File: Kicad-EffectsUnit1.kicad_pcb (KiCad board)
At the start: 2 copper layers, 100 x 100 mm, 175 parts, among them J101 In7, J102 Doepfer connector, J104 In6, J105 In3, J106 Out10, J107 Out11, J108 Out9, J109 Out6, J201 In, J202 Out, J203 Conn_01x02_Male, P201 HEADER_2x5_Doepfer, P301 HEADER_2x5_Doepfer, Q201 BC337, Q202 PZT2222A, Q203 PZT2222A, Q301 BC337, SW101 Dist 6, SW102 Crush A6, SW104 Rotary_Encoder_Switch, SW105 Dist 10, U101 TL072, U102 TL072, U201 L7805, U202 PT2399

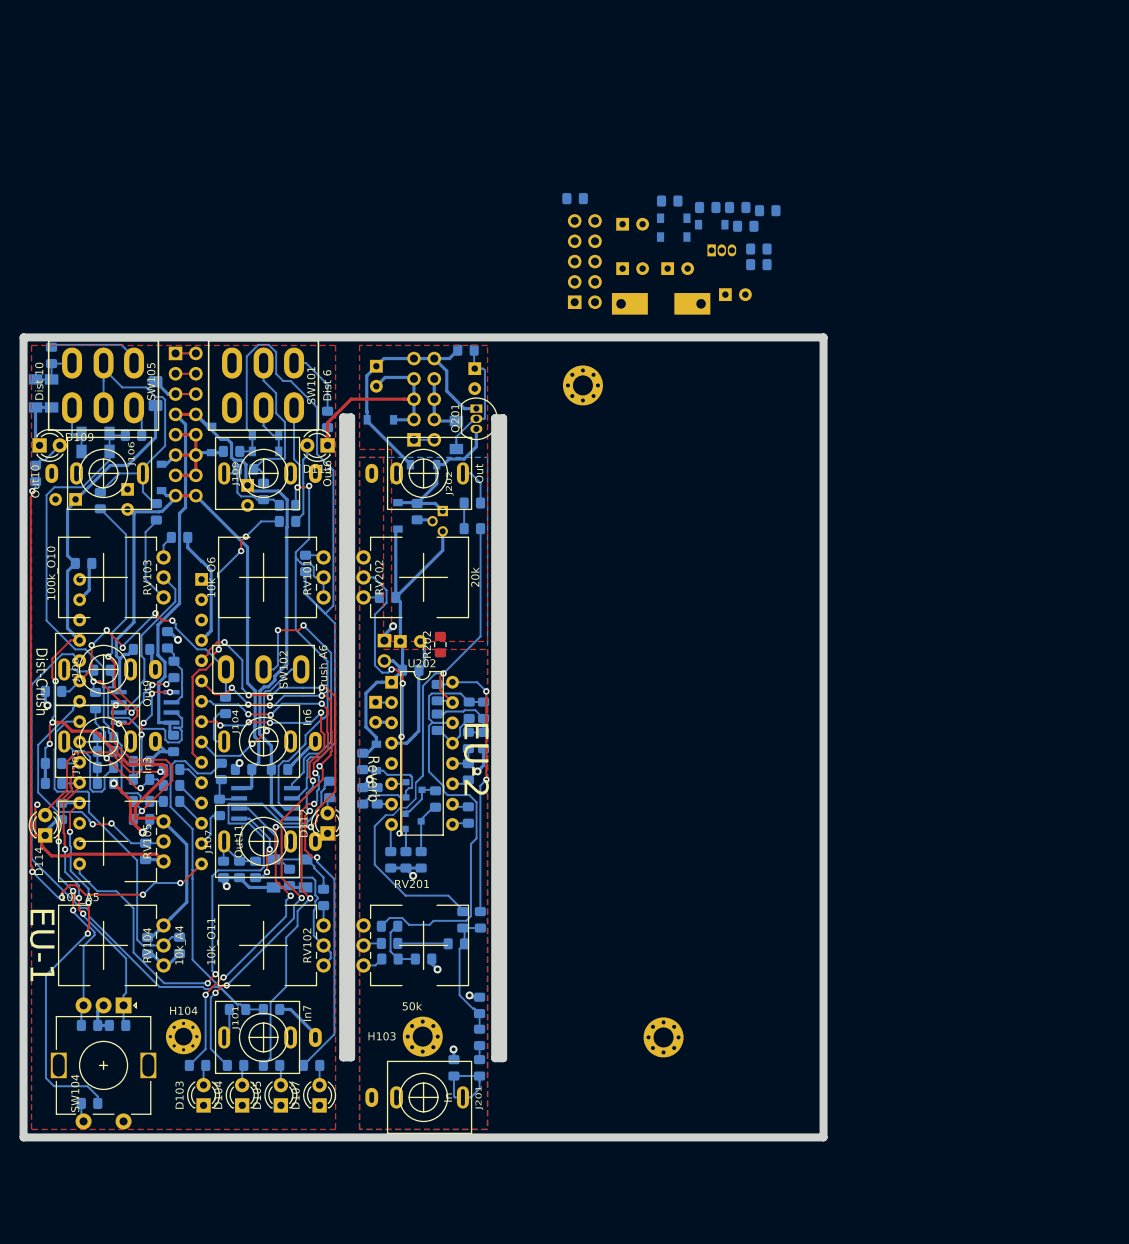
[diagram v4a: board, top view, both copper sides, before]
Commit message: Large components placed EU3
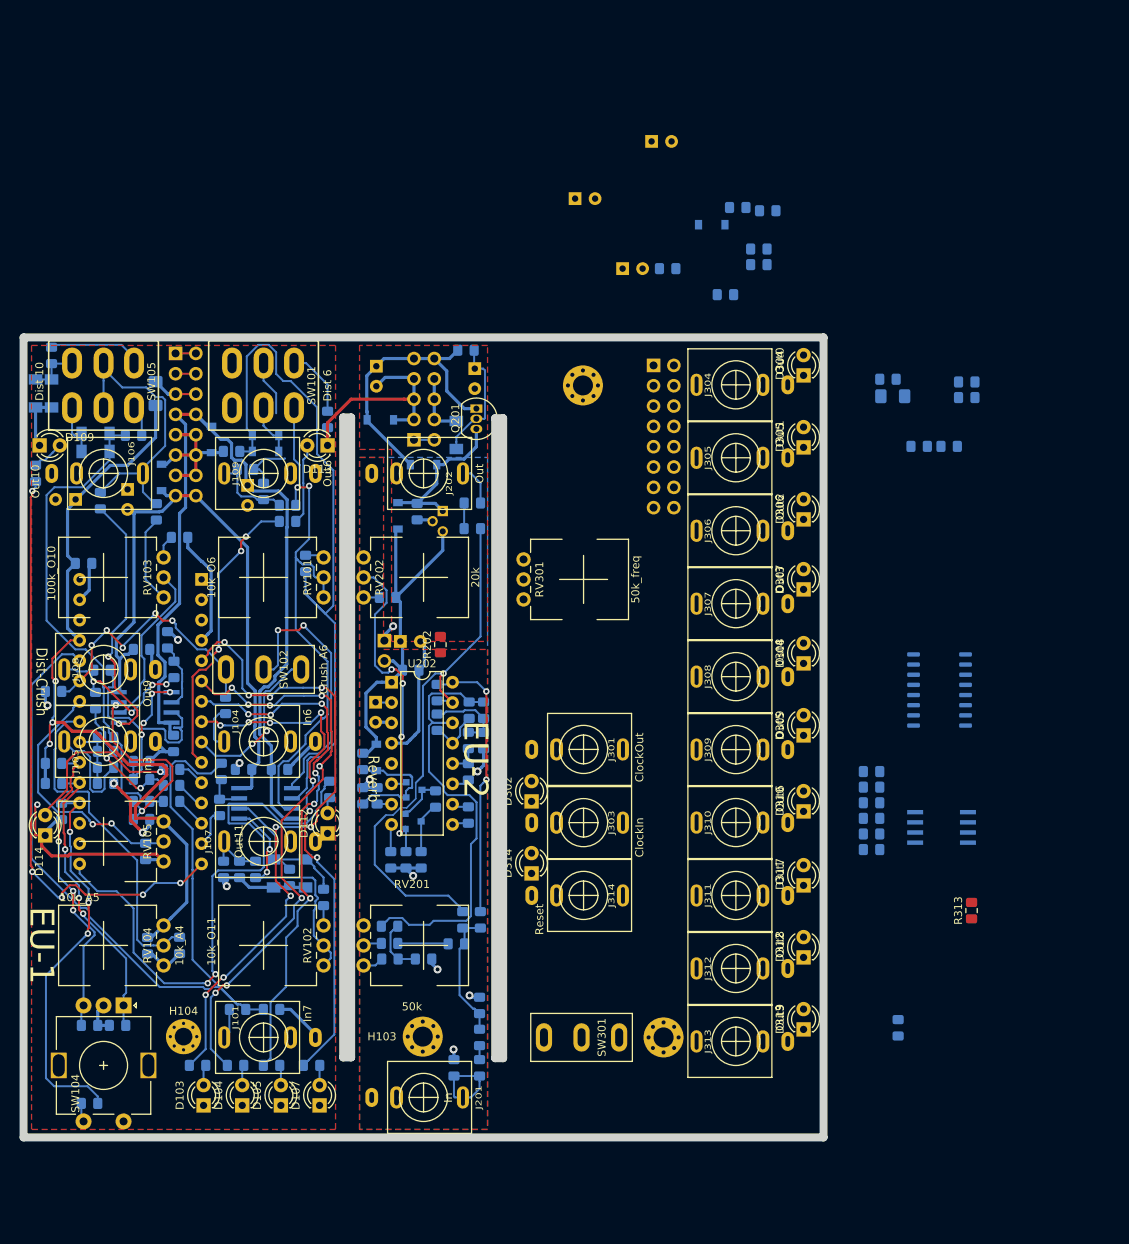
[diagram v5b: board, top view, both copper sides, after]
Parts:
- removed C306: 100uF 16v, Capacitor_THT:CP_Radial_D5.0mm_P2.50mm
- removed C307, C308: 100n, Capacitor_SMD:C_0805_2012Metric_Pad1.15x1.40mm_HandSolder
- removed D303: 1N1007, Diode_SMD:D_SOD-123
- removed P301: HEADER_2x5_Doepfer, Connector_PinHeader_2.54mm:PinHeader_2x05_P2.54mm_Vertical
- removed Q301: BC337, Package_TO_SOT_THT:TO-92_Inline
- added D305: LED_1, LED_THT:LED_D3.0mm, F.Cu at (197.5, 63.8)
- added D306: LED_2, LED_THT:LED_D3.0mm, F.Cu at (197.5, 72.8)
- added D307: LED_3, LED_THT:LED_D3.0mm, F.Cu at (197.5, 81.5)
- added D308: LED_4, LED_THT:LED_D3.0mm, F.Cu at (197.5, 90.8)
- added D309: LED_5, LED_THT:LED_D3.0mm, F.Cu at (197.5, 99.8)
- added D310: LED_6, LED_THT:LED_D3.0mm, F.Cu at (197.5, 109.2)
- added D311: LED_7, LED_THT:LED_D3.0mm, F.Cu at (197.5, 118.5)
- added D312: LED_8, LED_THT:LED_D3.0mm, F.Cu at (197.5, 127.5)
- added D313: LED_9, LED_THT:LED_D3.0mm, F.Cu at (197.5, 136.5)
- added D314: LED_RST, LED_THT:LED_D3.0mm, F.Cu at (163.5, 117.0)
- added F301: Polyfuse, Fuse:Fuse_1206_3216Metric_Pad1.42x1.75mm_HandSolder, B.Cu at (208.6, 57.3)
- added J301: ClockOut, AJ-Dropbox-Kicad:PJ301SM, F.Cu at (170.0, 101.5)
- added J302: Doepfer connector, Connector_PinSocket_2.54mm:PinSocket_2x08_P2.54mm_Vertical, B.Cu at (178.8, 53.5)
- added J303: ClockIn, AJ-Dropbox-Kicad:PJ301SM, F.Cu at (170.0, 110.7)
- added J304: Out0, AJ-Dropbox-Kicad:PJ301SM, F.Cu at (189.0, 55.9)
- added J305: Out1, AJ-Dropbox-Kicad:PJ301SM, F.Cu at (189.0, 65.0)
- added J306: Out2, AJ-Dropbox-Kicad:PJ301SM, F.Cu at (189.0, 74.2)
- added J307: Out3, AJ-Dropbox-Kicad:PJ301SM, F.Cu at (189.0, 83.3)
- added J308: Out4, AJ-Dropbox-Kicad:PJ301SM, F.Cu at (189.0, 92.4)
- added J309: Out5, AJ-Dropbox-Kicad:PJ301SM, F.Cu at (189.0, 101.5)
- added J310: Out6, AJ-Dropbox-Kicad:PJ301SM, F.Cu at (189.0, 110.6)
- added J311: Out7, AJ-Dropbox-Kicad:PJ301SM, F.Cu at (189.0, 119.8)
- added J312: Out8, AJ-Dropbox-Kicad:PJ301SM, F.Cu at (189.0, 128.9)
- added J313: Out9, AJ-Dropbox-Kicad:PJ301SM, F.Cu at (189.0, 138.0)
- added J314: Reset, AJ-Dropbox-Kicad:PJ301SM, F.Cu at (170.0, 119.8)
- added R303: 680R, Resistor_SMD:R_0805_2012Metric_Pad1.15x1.40mm_HandSolder, B.Cu at (208.0, 55.2)
- added R304: 680R, Resistor_SMD:R_0805_2012Metric_Pad1.15x1.40mm_HandSolder, B.Cu at (217.9, 57.5)
- added R305: 680R, Resistor_SMD:R_0805_2012Metric_Pad1.15x1.40mm_HandSolder, B.Cu at (215.7, 63.6)
- added R306: 680R, Resistor_SMD:R_0805_2012Metric_Pad1.15x1.40mm_HandSolder, B.Cu at (217.9, 55.6)
- added R307: 680R, Resistor_SMD:R_0805_2012Metric_Pad1.15x1.40mm_HandSolder, B.Cu at (206.0, 114.0)
- added R308: 220k, Resistor_SMD:R_0805_2012Metric_Pad1.15x1.40mm_HandSolder, B.Cu at (206.0, 112.1)
- added R309: 3k3, Resistor_SMD:R_0805_2012Metric_Pad1.15x1.40mm_HandSolder, B.Cu at (211.9, 63.6)
- added R310: 680R, Resistor_SMD:R_0805_2012Metric_Pad1.15x1.40mm_HandSolder, B.Cu at (206.0, 104.3)
- added R311: 10k, Resistor_SMD:R_0805_2012Metric_Pad1.15x1.40mm_HandSolder, B.Cu at (209.3, 136.3)
- added R312: 680R, Resistor_SMD:R_0805_2012Metric_Pad1.15x1.40mm_HandSolder, B.Cu at (206.0, 106.2)
- added R313: 680R, Resistor_SMD:R_0805_2012Metric_Pad1.15x1.40mm_HandSolder, F.Cu at (218.5, 121.6)
- added R314: 680R, Resistor_SMD:R_0805_2012Metric_Pad1.15x1.40mm_HandSolder, B.Cu at (206.0, 108.2)
- added R315: 680R, Resistor_SMD:R_0805_2012Metric_Pad1.15x1.40mm_HandSolder, B.Cu at (206.0, 110.1)
- added RV301: 50k_freq, Potentiometer_THT:Potentiometer_China_RK09_Single_Vertical_AJ, F.Cu at (162.5, 82.8)
- added SW301: Run, AJ-Dropbox-Kicad:SP1MS1, F.Cu at (169.8, 137.5)
- added U302: LM555, AJ-Dropbox-Kicad:AJ_SO-8_5.3x6.2mm_P1.27mm, B.Cu at (214.8, 111.2)
- added U303: 4017, Package_SO:SOIC-16_4.55x10.3mm_P1.27mm, B.Cu at (214.5, 94.1)
- C301, C305: value 100uF 16v -> 100n; footprint Capacitor_THT:CP_Radial_D5.0mm_P2.50mm -> Capacitor_SMD:C_0805_2012Metric_Pad1.15x1.40mm_HandSolder
- C302: value 100n -> 100uF; footprint Capacitor_SMD:C_0805_2012Metric_Pad1.15x1.40mm_HandSolder -> Capacitor_THT:CP_Radial_D5.0mm_P2.50mm
- C303: value 100n -> 100uF 16v; footprint Capacitor_SMD:C_0805_2012Metric_Pad1.15x1.40mm_HandSolder -> Capacitor_THT:CP_Radial_D5.0mm_P2.50mm
- C309: value 100n -> 10n
- D302: value 1N1007 -> LED_Clk; footprint Diode_SMD:D_SOD-123 -> LED_THT:LED_D3.0mm; moved to F.Cu
- D304: value 5v6 -> LED_0; footprint Diode_SMD:D_MELF-RM10_Universal_Handsoldering -> LED_THT:LED_D3.0mm; moved to F.Cu
- R301: value 10k -> 680R
- R302: value 0R -> 680R
- moved D302 75.0 mm to (163.5, 108.0), turned to 90 degrees
- moved D304 19.9 mm to (197.5, 54.8), turned to 90 degrees
- moved C303 7.79 mm to (178.5, 25.5)
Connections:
- net +9V renamed Net-(C203-Pad2)
- C301 pad 1: +12Vc -> GNDS
- C301 pad 2: GNDS -> +5V
- C302 pad 1: GNDS -> +5V
- C302 pad 2: +12Vc -> GNDS
- C303 pad 1: GNDS -> +12Vc
- C303 pad 2: +12Vc -> GNDS
- C305 pad 1: +5VL -> GNDS
- C305 pad 2: GNDS -> +12Vc
- C309 pad 1: -12Vc -> GNDS
- C309 pad 2: GNDS -> Net-(C309-Pad2)
- D301 pad 2: +5VL -> GNDS
- D302 pad 1: +12Vc -> GNDS
- D302 pad 2: GNDS -> Net-(D302-Pad2)
- D304 pad 1: Net-(C310-Pad1) -> GNDS
- D304 pad 2: GNDS -> Net-(D304-Pad2)
- R301 pad 1: Net-(C310-Pad1) -> ClockIn
- R301 pad 2: +12Vc -> Net-(D302-Pad2)
- R302 pad 1: GNDS -> Out0
- R302 pad 2: GNDS -> Net-(D304-Pad2)
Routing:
- net Net-(D110-Pad1): track 20.1 -> 14.0 mm

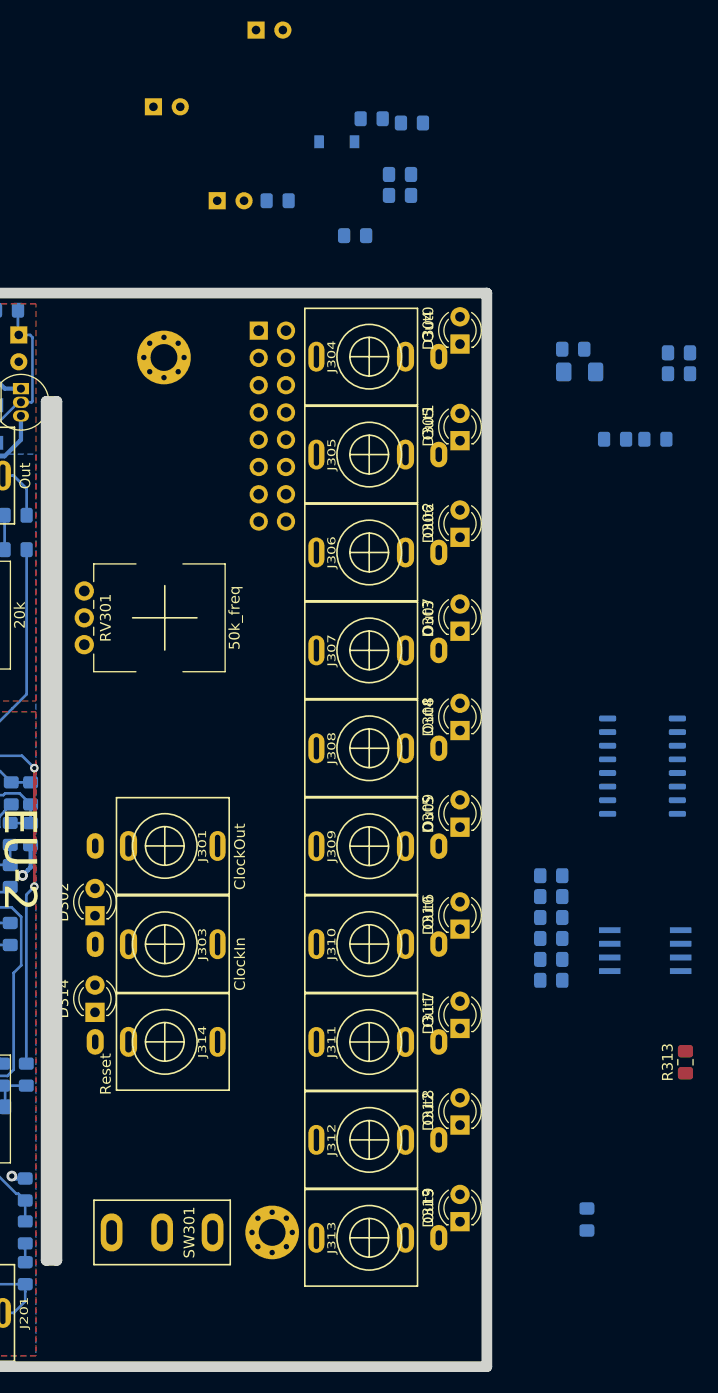
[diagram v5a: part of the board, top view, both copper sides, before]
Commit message: EU3 placed and routed
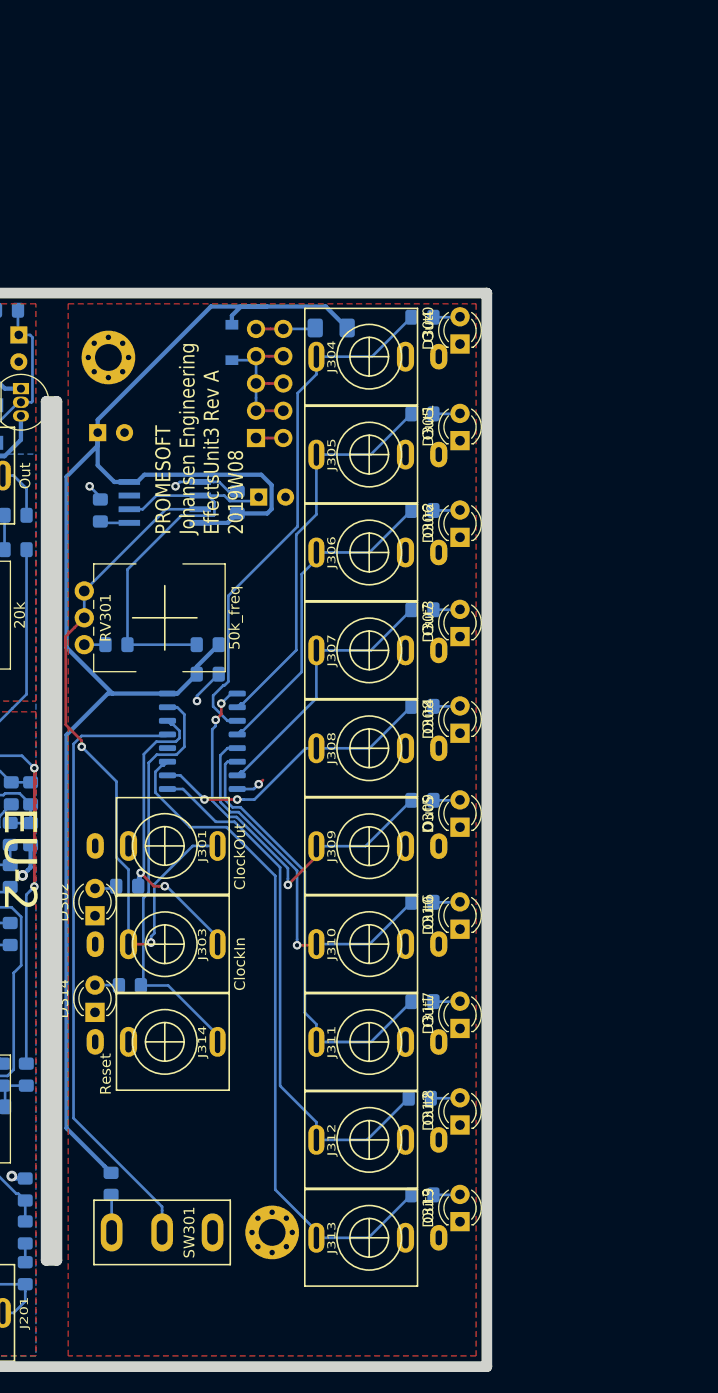
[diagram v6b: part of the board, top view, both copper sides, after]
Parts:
- removed C301: 100n, Capacitor_SMD:C_0805_2012Metric_Pad1.15x1.40mm_HandSolder
- removed C302: 100uF, Capacitor_THT:CP_Radial_D5.0mm_P2.50mm
- removed J302: Doepfer connector, Connector_PinSocket_2.54mm:PinSocket_2x08_P2.54mm_Vertical
- added P301: HEADER_2x5_Doepfer, Connector_PinHeader_2.54mm:PinHeader_2x05_P2.54mm_Vertical, B.Cu at (178.5, 63.5)
- R313: moved to B.Cu
- moved R301 75.0 mm to (166.5, 105.2), turned to 180 degrees
- moved U302 61.2 mm to (170.0, 69.5), turned to 180 degrees
- moved R309 50.2 mm to (165.5, 82.8)
- moved C305 44.6 mm to (174.0, 85.5), turned to 180 degrees
- moved R311 44.4 mm to (165.0, 133.0), turned to 270 degrees
- moved R308 43.4 mm to (174.0, 82.8), turned to 180 degrees
- moved C309 41.9 mm to (164.0, 70.2), turned to 270 degrees
- moved U303 41.1 mm to (173.5, 91.8), turned to 180 degrees
- moved R306 40.7 mm to (194.0, 88.5)
- moved C303 40.3 mm to (163.8, 63.0)
- moved R315 39.5 mm to (166.8, 114.5), turned to 180 degrees
- moved C304 32.4 mm to (176.8, 69.5), turned to 270 degrees
- moved R314 28.5 mm to (194.0, 134.0)
- moved C310 27.9 mm to (178.8, 69.0)
- moved R304 27.1 mm to (194.0, 70.2)
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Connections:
- F301 pad 1: /EU3/+5Vin -> Net-(F301-Pad1)
- F301 pad 2: +5V -> +12Vc
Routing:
- net +12Vc: track 0.00 -> 151.9 mm
- net ClockOut: track 0.00 -> 65.1 mm, vias 0 -> 2
- net Out9: track 3.63 -> 67.3 mm
- net Net-(SW301-Pad2): track 0.00 -> 58.0 mm
- net Out8: track 0.00 -> 51.2 mm
- net Out0: track 0.00 -> 49.8 mm
- net Out7: track 0.00 -> 41.5 mm
- net Reset: track 0.00 -> 39.6 mm
- net Net-(C310-Pad1): track 0.00 -> 39.4 mm
- net Out5: track 0.00 -> 37.8 mm, vias 0 -> 3
- net Out1: track 0.00 -> 37.1 mm
- net Out6: track 20.9 -> 56.2 mm, vias 2 -> 3
- net Out2: track 0.00 -> 30.6 mm
- net ClockIn: track 0.00 -> 30.3 mm, vias 0 -> 2
- net GNDS: track 0.00 -> 29.1 mm, vias 0 -> 4
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- added copper zone on F.Cu, net GNDS
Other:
- board text added: "+5v +12v GND GND GND -12V"
- board text added: "PROMESOFT Johansen Engineering EffectsUnit3 Rev A 2019W08"
- board text removed: "PROMESOFT Johansen Engineering EffectsUnit1 Rev A 2019W08"

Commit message: Labels
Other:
- board text added: "Clock - Count"
- board text added: "EU-3"

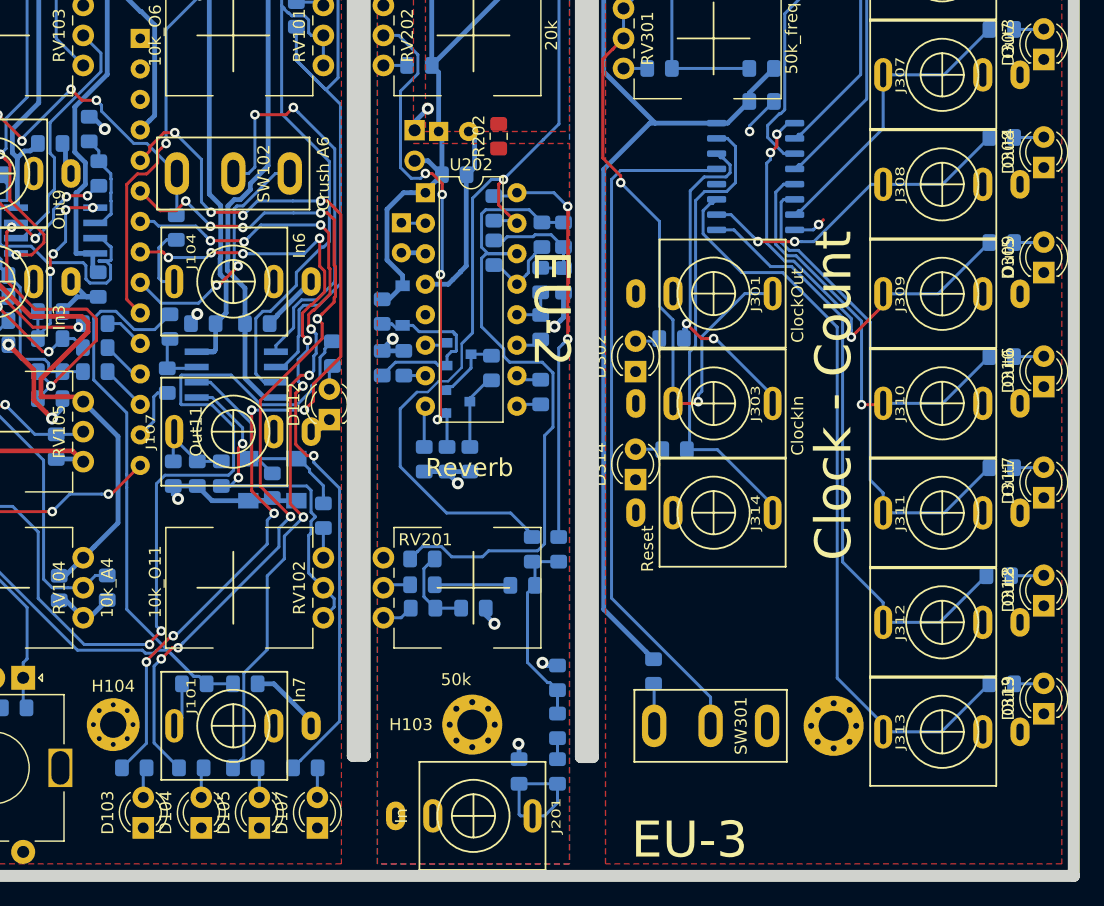
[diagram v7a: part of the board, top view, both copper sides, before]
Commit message: Labels and logos done
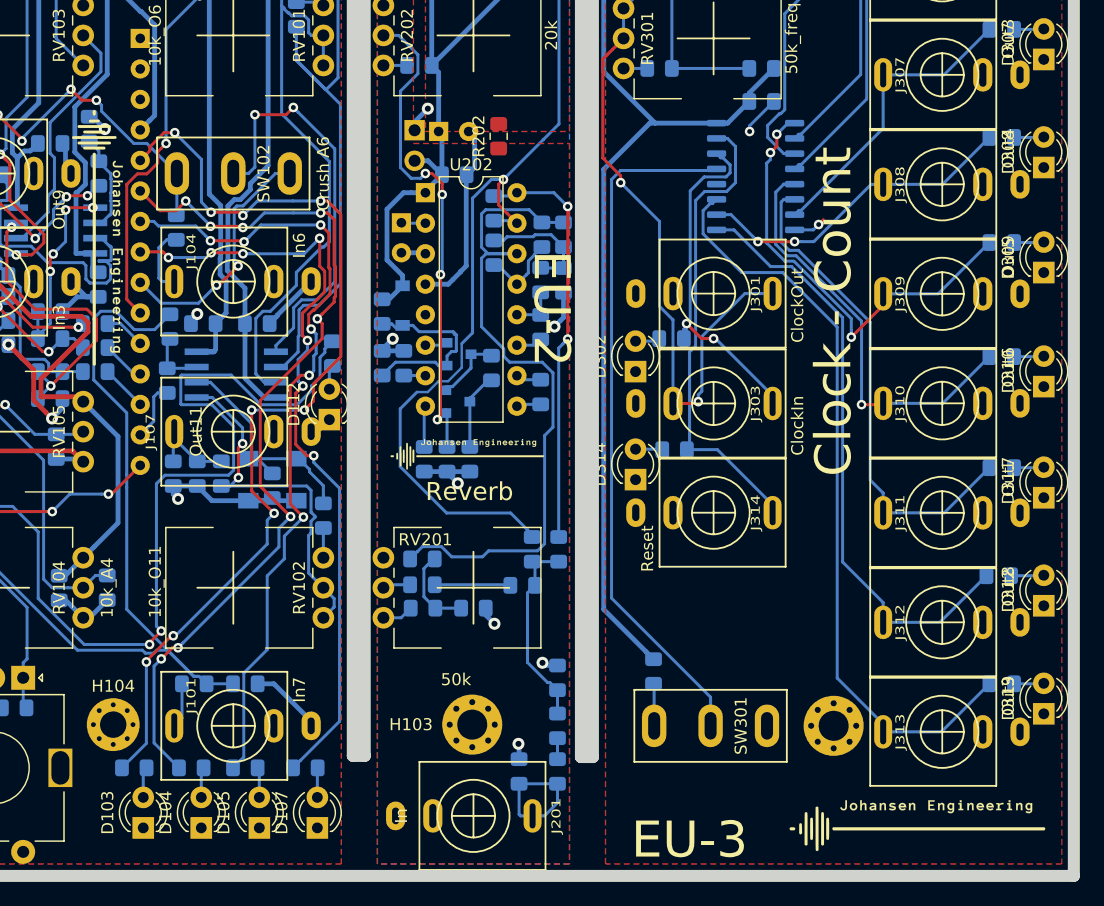
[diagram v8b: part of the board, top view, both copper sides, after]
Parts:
- added G***: LOGO, AJ:Johansen_engineering_logo_25mm_front_neg5, B.Cu at (102.5, 126.0)
- added G***: LOGO, AJ:Johansen_engineering_logo_25mm_front_neg5, F.Cu at (118.5, 96.9)
- added G***: LOGO, AJ:Johansen_engineering_logo_25mm_front_neg5, F.Cu at (187.0, 146.0)
- added G***: LOGO, AJ:Johansen_engineering_logo_25mm_front_neg5, B.Cu at (189.0, 101.5)
- added G***: LOGO, AJ:Johansen_engineering_logo_15mm, F.Cu at (149.5, 115.0)
- added G***: LOGO, AJ:Johansen_engineering_logo_15mm, B.Cu at (144.0, 136.5)
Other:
- board text added: "JE 2019W08"
- board text removed: "PROMESOFT 2019W08 Johansen Engineering"
